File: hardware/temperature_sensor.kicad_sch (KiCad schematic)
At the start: 12 parts

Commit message: Add the Cube project
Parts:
- removed C? (x2): 100n, Capacitor_SMD:C_0603_1608Metric, symbol Device:C_Small
- removed C?: 1n, Capacitor_SMD:C_0603_1608Metric, symbol Device:C_Small
- removed R? (x5): 10k, Resistor_SMD:R_0603_1608Metric, symbol Device:R
- removed R? (x2): 47k, Resistor_SMD:R_0603_1608Metric, symbol Device:R
- removed R?: 22R, Resistor_SMD:R_0603_1608Metric, symbol Device:R
- removed U?: TSX7191, Package_TO_SOT_SMD:SOT-23-5, symbol Amplifier_Operational:OPA340NA
- added C? (x2): 1n, Capacitor_SMD:C_0603_1608Metric, symbol Device:C_Small
- added C?: 100n, Capacitor_SMD:C_0603_1608Metric, symbol Device:C_Small
- added R? (x4): 4k7, Resistor_SMD:R_0603_1608Metric, symbol Device:R
- added R?: 8k5, Resistor_SMD:R_0603_1608Metric, symbol Device:R
- added R?: 22R, Resistor_SMD:R_0603_1608Metric, symbol Device:R
- added R? (x2): 150k, Resistor_SMD:R_0603_1608Metric, symbol Device:R
- added U?: TSX7191, Package_TO_SOT_SMD:SOT-23-5, symbol Amplifier_Operational:OPA340NA
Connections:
- net +3.3VA: now also C?.2, R?.1, R?.1, U?.5 (V+)
- net GND: now also C?.1, C?.1, R?.2, R?.2, U?.2 (V-)
- net IN: now also R?.2, R?.2
- net IN+: now also R?.1, R?.2, R?.2
- net OUT: now also R?.1
- new net: C?.2, R?.1, R?.1, U?.3 (+)
- new net: C?.2, R?.1, R?.2, U?.4 (-)
- new net: C?.1, R?.1, R?.2, U?.1
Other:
- note added: "5k"
- note removed: "External connector"
- note removed: "NTC"

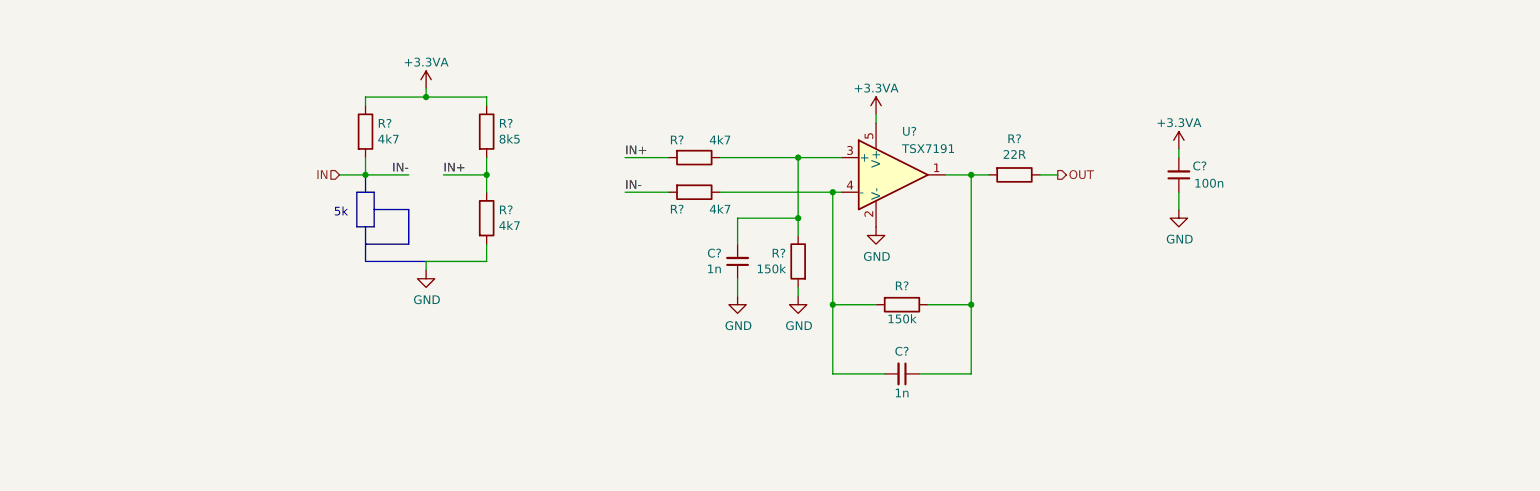
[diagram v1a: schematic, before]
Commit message: Improve the schematic
- add anti-aliasing filters
- rearrange the main connector signals
- improve the power filtering
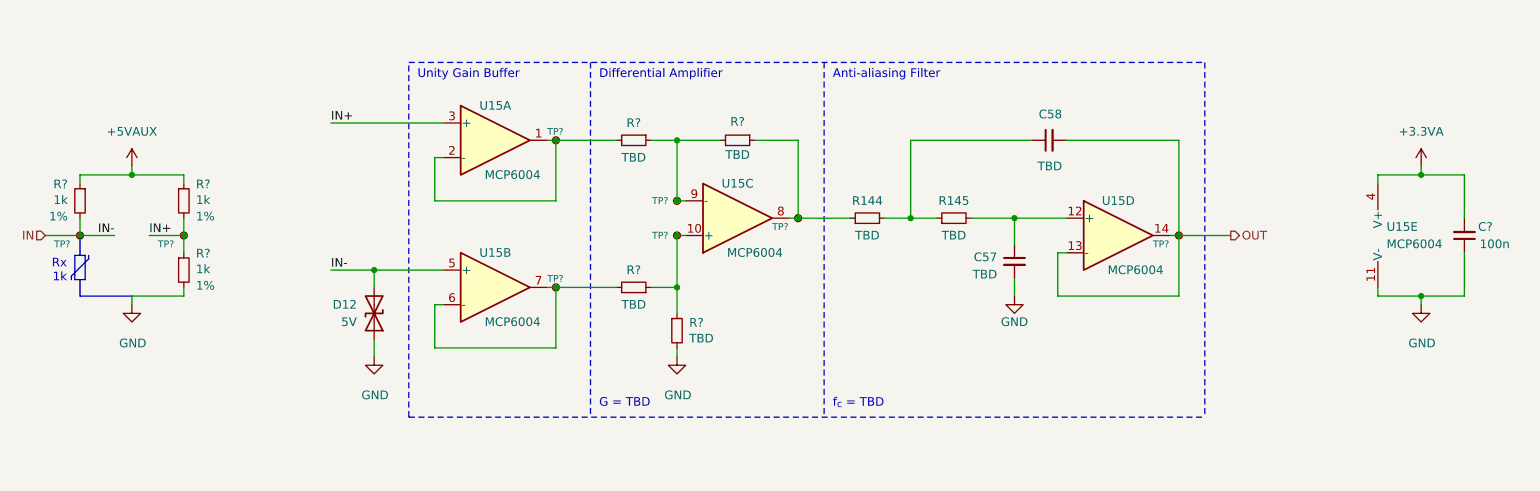
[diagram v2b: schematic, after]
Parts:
- removed C? (x2): 1n, Capacitor_SMD:C_0603_1608Metric, symbol Device:C_Small
- removed C?: 100n, Capacitor_SMD:C_0603_1608Metric, symbol Device:C_Small
- removed R? (x4): 4k7, Resistor_SMD:R_0603_1608Metric, symbol Device:R
- removed R?: 8k5, Resistor_SMD:R_0603_1608Metric, symbol Device:R
- removed R?: 22R, Resistor_SMD:R_0603_1608Metric, symbol Device:R
- removed R? (x2): 150k, Resistor_SMD:R_0603_1608Metric, symbol Device:R
- removed U?: TSX7191, Package_TO_SOT_SMD:SOT-23-5, symbol Amplifier_Operational:OPA340NA
- added C57, C58: TBD, Capacitor_SMD:C_0603_1608Metric_Pad1.08x0.95mm_HandSolder, symbol Device:C_Small
- added C?: 100n, Capacitor_SMD:C_0603_1608Metric, symbol Device:C_Small
- added D12: 5V, symbol Device:D_TVS
- added R144, R145: TBD, Resistor_SMD:R_0603_1608Metric_Pad0.98x0.95mm_HandSolder, symbol Device:R_Small
- added R? (x4): TBD, Resistor_SMD:R_0603_1608Metric, symbol Device:R_Small
- added R? (x3): 1k, Resistor_SMD:R_0603_1608Metric, symbol Device:R_Small
- added TP? (x8): TestPoint_Small, TestPoint:TestPoint_Pad_D1.0mm, symbol Connector:TestPoint_Small
- added U15: MCP6004, symbol Amplifier_Operational:MCP6004
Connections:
- net +3.3VA: now also C?.2, U15.4 (V+)
- net GND: now also C57.2, C?.1, D12.1 (A1), R?.2, R?.2, U15.11 (V-)
- net IN: now also D12.2 (A2), R?.2, TP?.1, U15.5 (+)
- net IN+: now also R?.1, R?.2, TP?.1, U15.3 (+)
- net OUT: now also C58.2, TP?.1, U15.13 (-), U15.14
- new net: R?.1, R?.1, TP?.1, U15.10 (+)
- new net: R144.1, R?.1, TP?.1, U15.8
- new net: R?.1, R?.2, TP?.1, U15.9 (-)
- new net: R?.2, TP?.1, U15.6 (-), U15.7
- new net: C58.1, R144.2, R145.1
- new net: C57.1, R145.2, U15.12 (+)
- new net: R?.2, TP?.1, U15.1, U15.2 (-)
- new net +5VAUX: R?.1, R?.1
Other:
- note added: "Anti-aliasing Filter"
- note added: "Differential Amplifier"
- note added: "G = TBD"
- note added: "Rx 1k"
- note added: "Unity Gain Buffer"
- note added: "f_{c} = TBD"
- note removed: "5k"

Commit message: Set component values
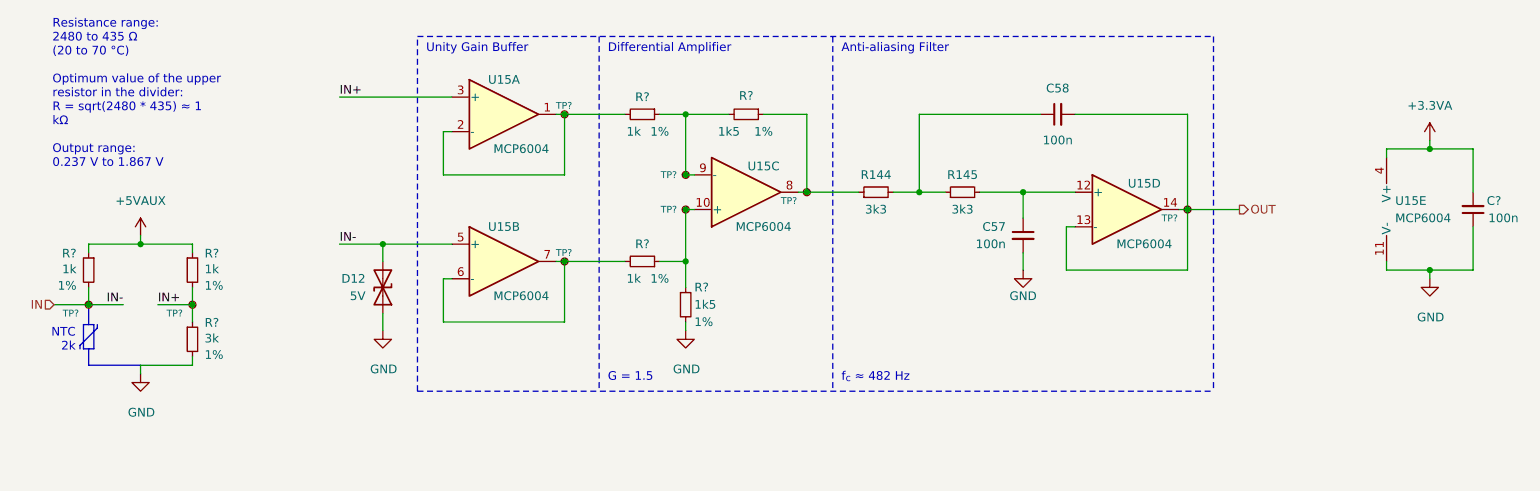
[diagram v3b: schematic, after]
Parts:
- C57, C58: value TBD -> 100n; footprint Capacitor_SMD:C_0603_1608Metric_Pad1.08x0.95mm_HandSolder -> Capacitor_SMD:C_0603_1608Metric
- R144, R145: value TBD -> 3k3; footprint Resistor_SMD:R_0603_1608Metric_Pad0.98x0.95mm_HandSolder -> Resistor_SMD:R_0603_1608Metric
- R? (x2): value TBD -> 1k5; Tolerance (none) -> 1%
- R?: value 1k -> 3k
- R? (x2): value TBD -> 1k; Tolerance (none) -> 1%
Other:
- note added: "G = 1.5"
- note added: "NTC 2k"
- note added: "f_{c} ≈ 482 Hz"
- note removed: "G = TBD"
- note removed: "Rx 1k"
- note removed: "f_{c} = TBD"
- moved on the sheet: C57, C58, C?, D12, R144, R145, R?, TP?, U15A, U15B, U15C, U15D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

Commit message: Improve the schematic according to the feedback
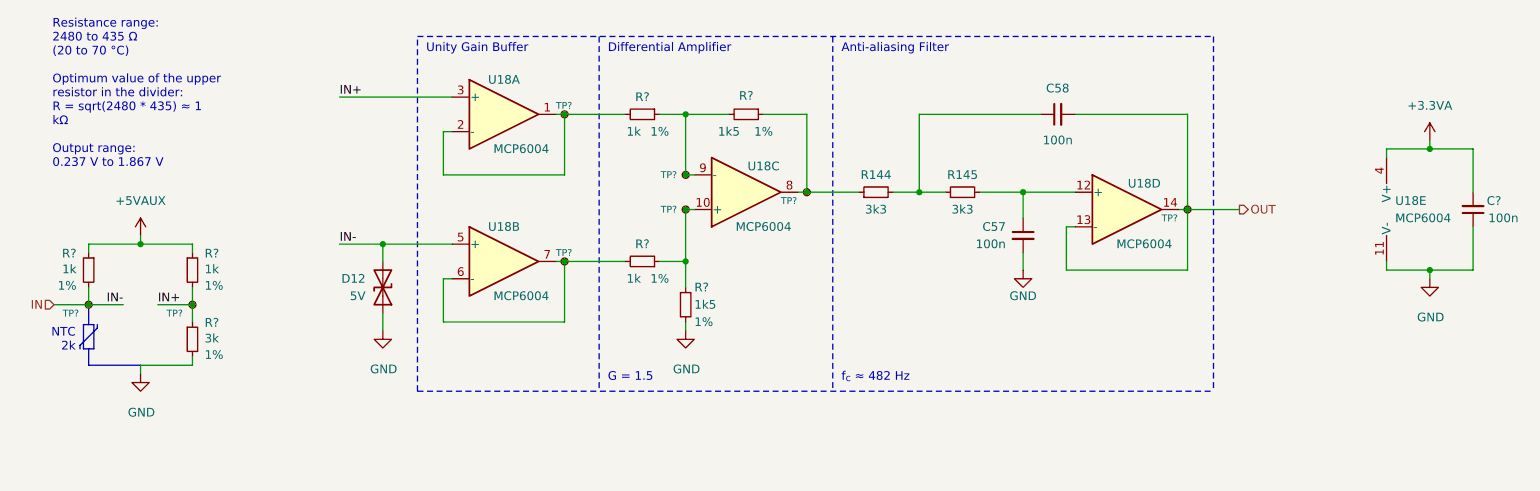
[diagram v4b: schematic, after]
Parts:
- renumbered U15 to U18

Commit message: Add high-side drivers to the fans and pumps
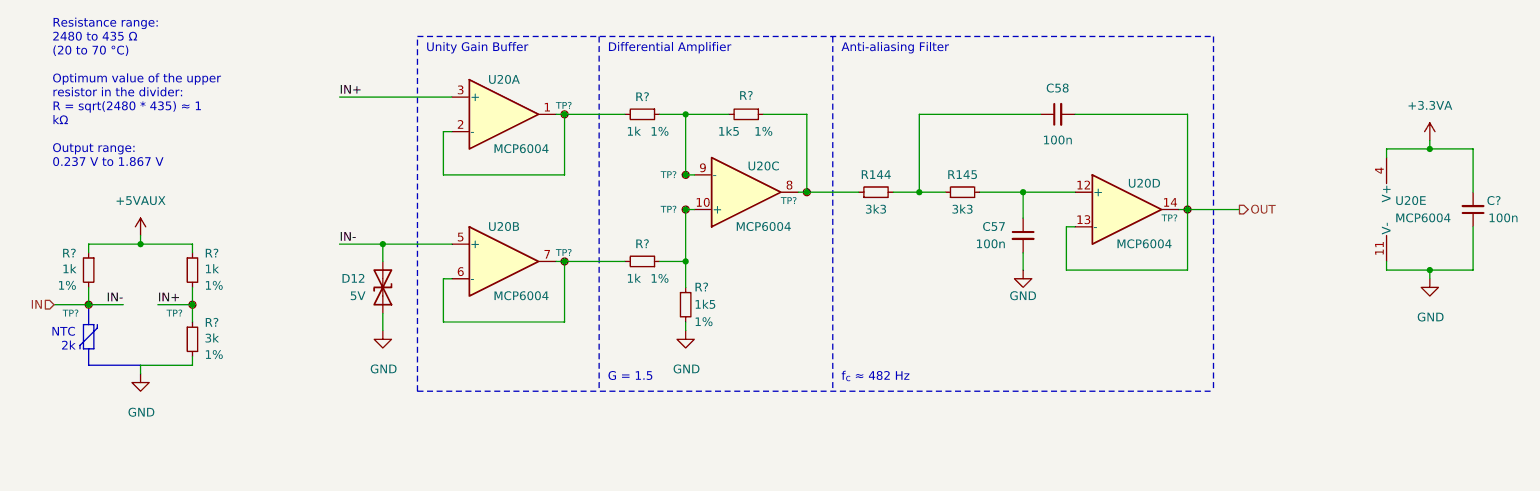
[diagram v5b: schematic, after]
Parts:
- renumbered U18 to U20

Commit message: Use in-amps
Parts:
- removed C57, C58, C?: 100n, Capacitor_SMD:C_0603_1608Metric, symbol Device:C_Small
- removed D12: 5V, symbol Device:D_TVS
- removed R144, R145: 3k3, Resistor_SMD:R_0603_1608Metric, symbol Device:R_Small
- removed R? (x2): 1k5, Resistor_SMD:R_0603_1608Metric, symbol Device:R_Small
- removed R? (x2): 1k, Resistor_SMD:R_0603_1608Metric, symbol Device:R_Small
- removed TP? (x6): TestPoint_Small, TestPoint:TestPoint_Pad_D1.0mm, symbol Connector:TestPoint_Small
- removed U20: MCP6004, symbol Amplifier_Operational:MCP6004
- added C? (x2): 100n, Capacitor_SMD:C_0603_1608Metric, symbol Device:C_Small
- added C? (x2): TBD, Capacitor_SMD:C_0603_1608Metric, symbol Device:C_Small
- added D14: 5V, symbol Device:D_TVS
- added NT1: NetTie_2, symbol Device:NetTie_2
- added R? (x4): TBD, Resistor_SMD:R_0603_1608Metric, symbol Device:R_Small
- added TP? (x4): TestPoint_Small, TestPoint:TestPoint_Pad_D1.0mm, symbol Connector:TestPoint_Small
- added U?: MCP6N11-005, Package_DFN_QFN:TDFN-8-1EP_3x2mm_P0.5mm_EP1.80x1.65mm, symbol MCP6N11:MCP6N11
- added U?: MCP6001, Package_TO_SOT_SMD:SOT-23-5, symbol Amplifier_Operational:MCP6001-OT
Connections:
- net +3.3VA: now also C?.1, C?.1, U?.5 (V+), U?.7 (V+), U?.8 (EN)
- net GND: now also C?.2, C?.2, C?.2, D14.1 (A1), R?.1, U?.2 (V-), U?.4 (V-), U?.5 (RF), U?.9 (EP)
- net IN: now also NT1.1; no longer R?.2, TP?.1
- net IN+: now also TP?.1, U?.2 (-)
- net OUT: now also C?.2, TP?.1, U?.1, U?.4 (-)
- new net: R?.1, R?.2, U?.1 (FG)
- new net: R?.1, R?.2, TP?.1, U?.6
- new net: C?.1, R?.1, R?.2
- new net: C?.1, R?.2, U?.3 (+)
- new net IN-: D14.2 (A2), NT1.2, R?.2, TP?.1, TP?.1, U?.3 (+)
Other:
- note added: "G = TBD"
- note added: "Instrumentation Amplifier"
- note added: "f_{c} = TBD"
- note removed: "Differential Amplifier"
- note removed: "G = 1.5"
- note removed: "Unity Gain Buffer"
- note removed: "f_{c} ≈ 482 Hz"

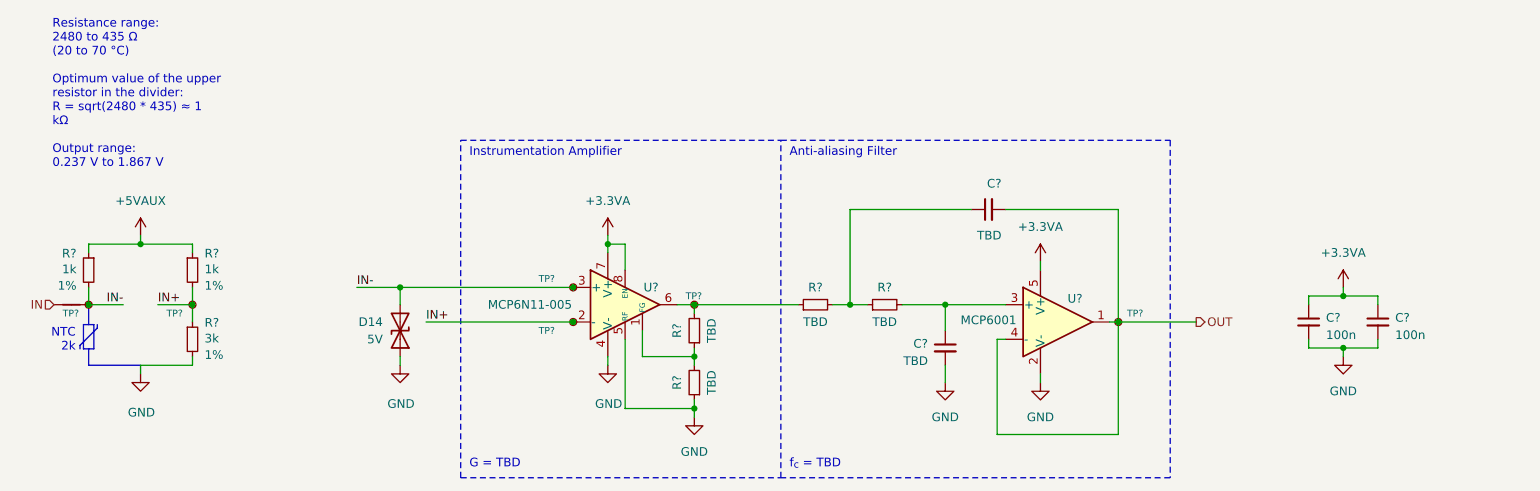
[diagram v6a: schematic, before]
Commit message: Improve the diagram based on the feedback
- add an input LC filter
- remove the USB connector
- add a programmer connector
- move optocouplers into a subsheet
- add a suspension tension meter IC
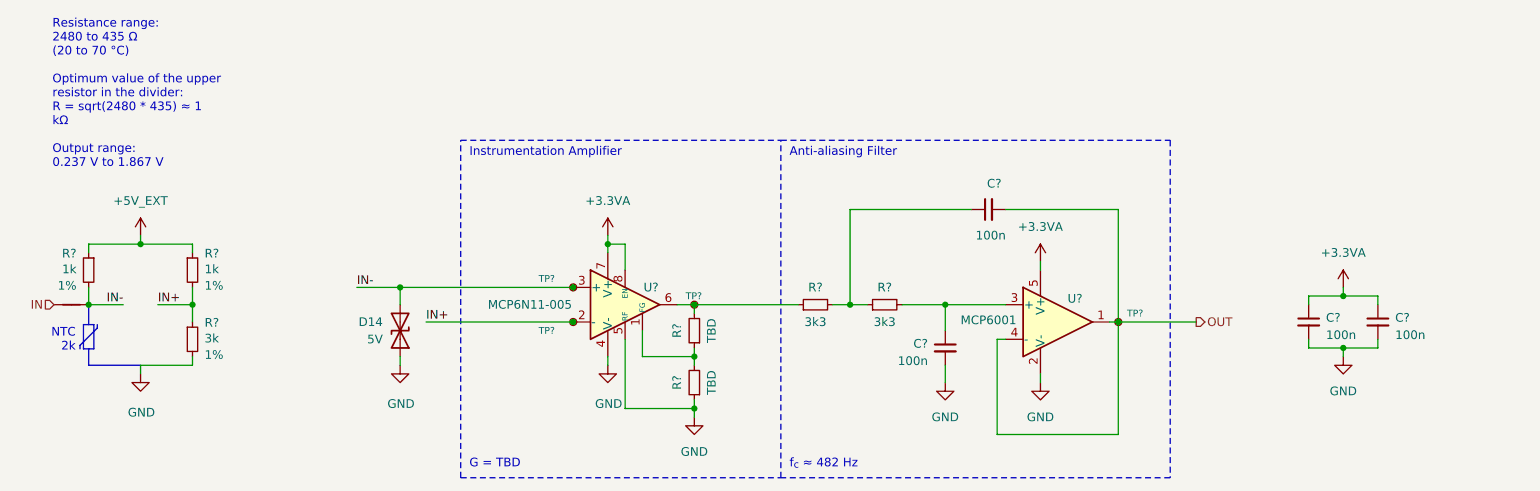
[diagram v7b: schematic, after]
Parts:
- removed TP? (x2): TestPoint_Small, TestPoint:TestPoint_Pad_D1.0mm, symbol Connector:TestPoint_Small
- C? (x2): value TBD -> 100n
- D14: footprint (none) -> Diode_SMD:D_SOD-523; Component (none) -> PESD5V0V1BB-QX
- NT1: footprint (none) -> NetTie:NetTie-2_SMD_Pad0.5mm
- R? (x2): value TBD -> 3k3
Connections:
- net +5VAUX renamed +5V_EXT
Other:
- note added: "f_{c} ≈ 482 Hz"
- note removed: "f_{c} = TBD"
- title: (none) -> Temperature Sensor
